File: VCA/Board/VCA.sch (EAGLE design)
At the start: 62 parts, among them IC1 TL074P, T1 BC237, T2 BC237, T3 BC237, T4 BC237, X1 1503_02, X2 1503_02, X3 1503_02, X4 1503_02

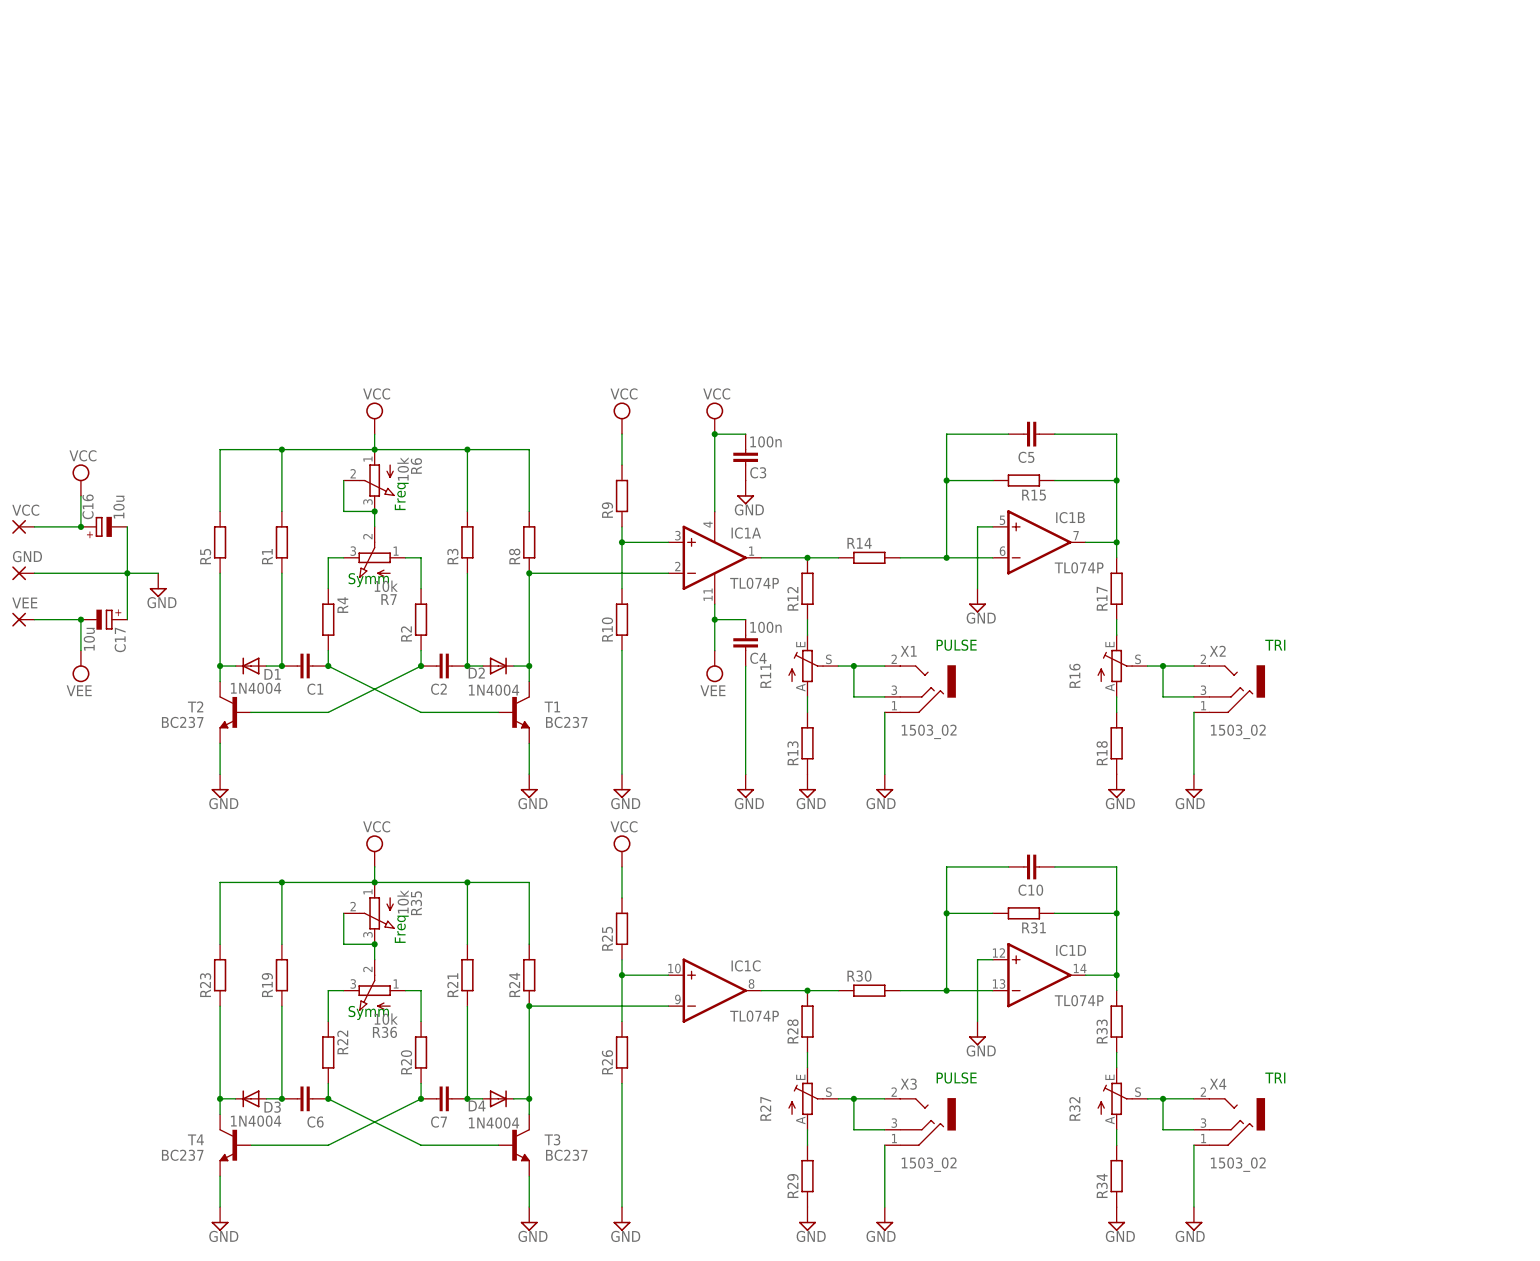
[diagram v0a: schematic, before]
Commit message: Add VCA schematic
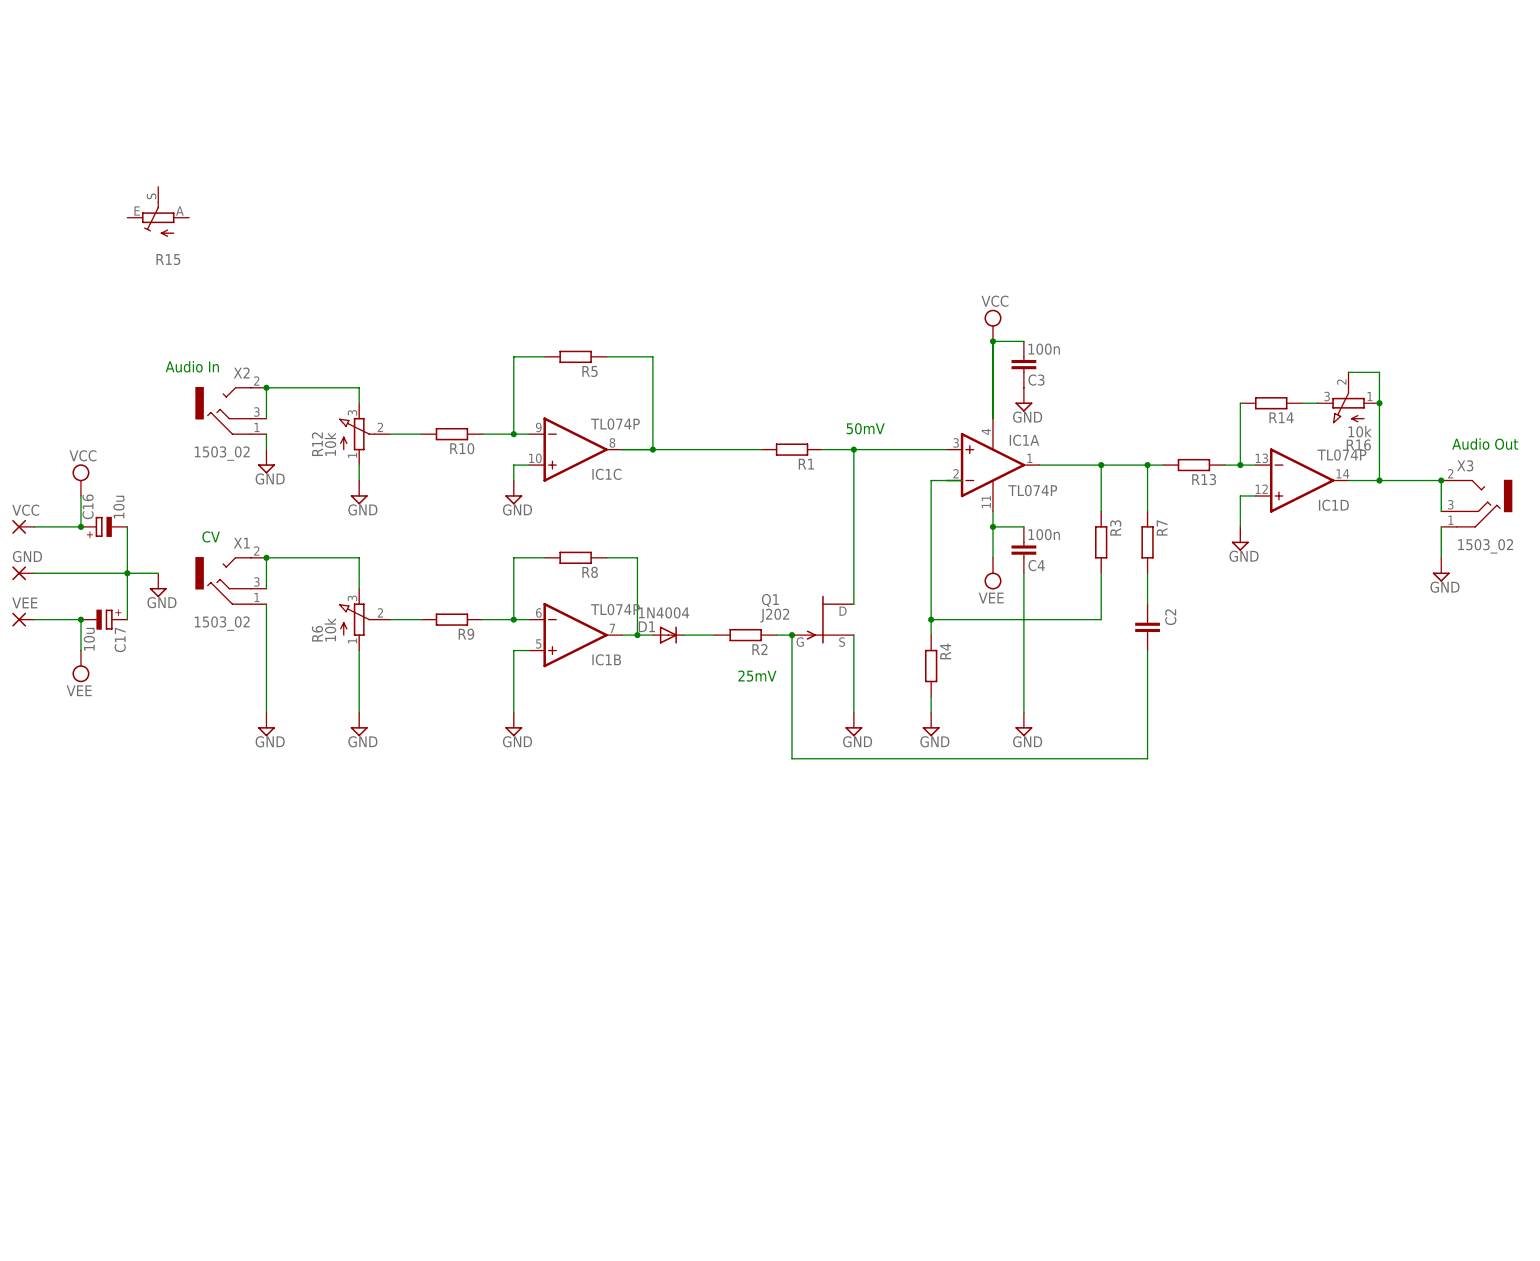
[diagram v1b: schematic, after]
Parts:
- removed C1, C10, C5, C6, C7: (no value), rcl:C-EU050-045X075
- removed D2, D3, D4: 1N4004, diode:1N4004
- removed R11, R27, R32: (no value), pot:TRIM_EU-S75P
- removed R17, R18, R19, R20, R21, R22, R23, R24, R25, R26, R28, R29, R30, R31, R33, R34: (no value), rcl:R-EU_0207/10
- removed R35, R36: 10k, pot:3RP/1610N
- removed T1, T2, T3, T4: BC237, transistor:BC237
- removed X4: 1503_02, con-lumberg:1503_02
- added Q1: J202, transistor-fet:J202
- R12: value (none) -> 10k; device rcl:R-EU_0207/10 -> pot:3RP/1610N
- R15: device rcl:R-EU_0207/10 -> pot:TRIM_EU-S75P
- R16: value (none) -> 10k; device pot:TRIM_EU-S75P -> pot:3RP/1610N
- R7: value 10k -> (none); device pot:3RP/1610N -> rcl:R-EU_0207/10
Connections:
- removed net N$18: D3.C, R23.1, T4.C
- removed net N$19: C6.2, D3.A, R19.1
- removed net N$20: R16.A, R18.2
- removed net N$21: R16.E, R17.1
- removed net N$22: C6.1, R22.2, T3.B
- removed net N$23: C7.2, R20.1, T4.B
- removed net N$24: C7.1, D4.A, R21.1
- removed net N$25: D4.C, IC1C.-IN, R24.1, T3.C
- removed net N$26: R22.1, R36.E
- removed net N$27: R20.2, R36.A
- removed net N$28: R35.E, R35.S, R36.S
- removed net N$29: IC1C.+IN, R25.1, R26.2
- removed net N$30: IC1C.OUT, R28.2, R30.1
- removed net N$31: R27.A, R29.2
- removed net N$32: R27.E, R28.1
- removed net N$33: C10.1, IC1D.OUT, R31.1, R33.2
- removed net N$34: C10.2, IC1D.-IN, R30.2, R31.2
- removed net N$35: R32.A, R34.2
- removed net N$36: R32.E, R33.1
- removed net N$37: R27.S, X3.2, X3.3
- removed net N$38: R32.S, X4.2, X4.3
- net GND: now also C3.1, C4.1, IC1C.+IN, Q1.S, R12.A, R4.2, R6.A; no longer R10.1, R13.1, R18.1, R26.1, R29.1, R34.1, T1.E, T2.E, T3.E, T4.E, X4.1
- net N$1: now also IC1A.+IN, Q1.D, R1.1; no longer C2.2, R2.1, T2.B
- net N$10: now also R12.E; no longer R16.S
- net N$11: now also IC1C.OUT, R1.2, R5.1; no longer IC1A.+IN, R10.2, R9.1
- net N$12: now also IC1C.-IN, R10.1, R5.2; no longer R11.A, R13.2
- net N$13: now also R10.2, R12.S; no longer IC1A.OUT, R12.2, R14.1
- net N$14: now also IC1D.-IN, R13.1, R14.2; no longer R11.E, R12.1
- net N$15: now also R6.E; no longer R11.S
- net N$16: now also R14.1, R16.E; no longer C5.1, IC1B.OUT, R15.1, R17.2
- net N$17: now also IC1D.OUT, R16.A, R16.S, X3.2, X3.3; no longer C5.2, IC1B.-IN, R14.2, R15.2
- net N$2: now also C2.2, Q1.G, R2.1; no longer C2.1, D2.A, R3.1
- net N$3: now also IC1A.-IN, R3.2, R4.1; no longer D1.C, R5.1, T2.C
- net N$4: now also IC1A.OUT, R13.2, R3.1, R7.1; no longer C1.2, D1.A, R1.1
- net N$5: now also C2.1, R7.2; no longer C1.1, R4.2, T1.B
- net N$6: now also R6.S, R9.2; no longer D2.C, IC1A.-IN, R8.1, T1.C
- net N$7: now also D1.A, IC1B.OUT, R8.1; no longer R4.1, R7.E
- net N$8: now also IC1B.-IN, R8.2, R9.1; no longer R2.2, R7.A
- net N$9: now also D1.C, R2.2; no longer R6.E, R6.S, R7.S
- net VCC: now also C3.2; no longer R1.2, R19.2, R21.2, R23.2, R24.2, R25.2, R3.2, R5.2, R8.2, R9.2
- net VEE: now also C4.2
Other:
- note added: "25mV"
- note added: "50mV"
- note added: "Audio In"
- note added: "Audio Out"
- note added: "CV"
- note removed: "Freq"
- note removed: "PULSE"
- note removed: "Symm"
- note removed: "TRI"
- moved on the sheet: C2, C3, C4, D1, IC1A, IC1B, IC1C, IC1D, R1, R10, R13, R14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

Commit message: Add clip indicator to VCA
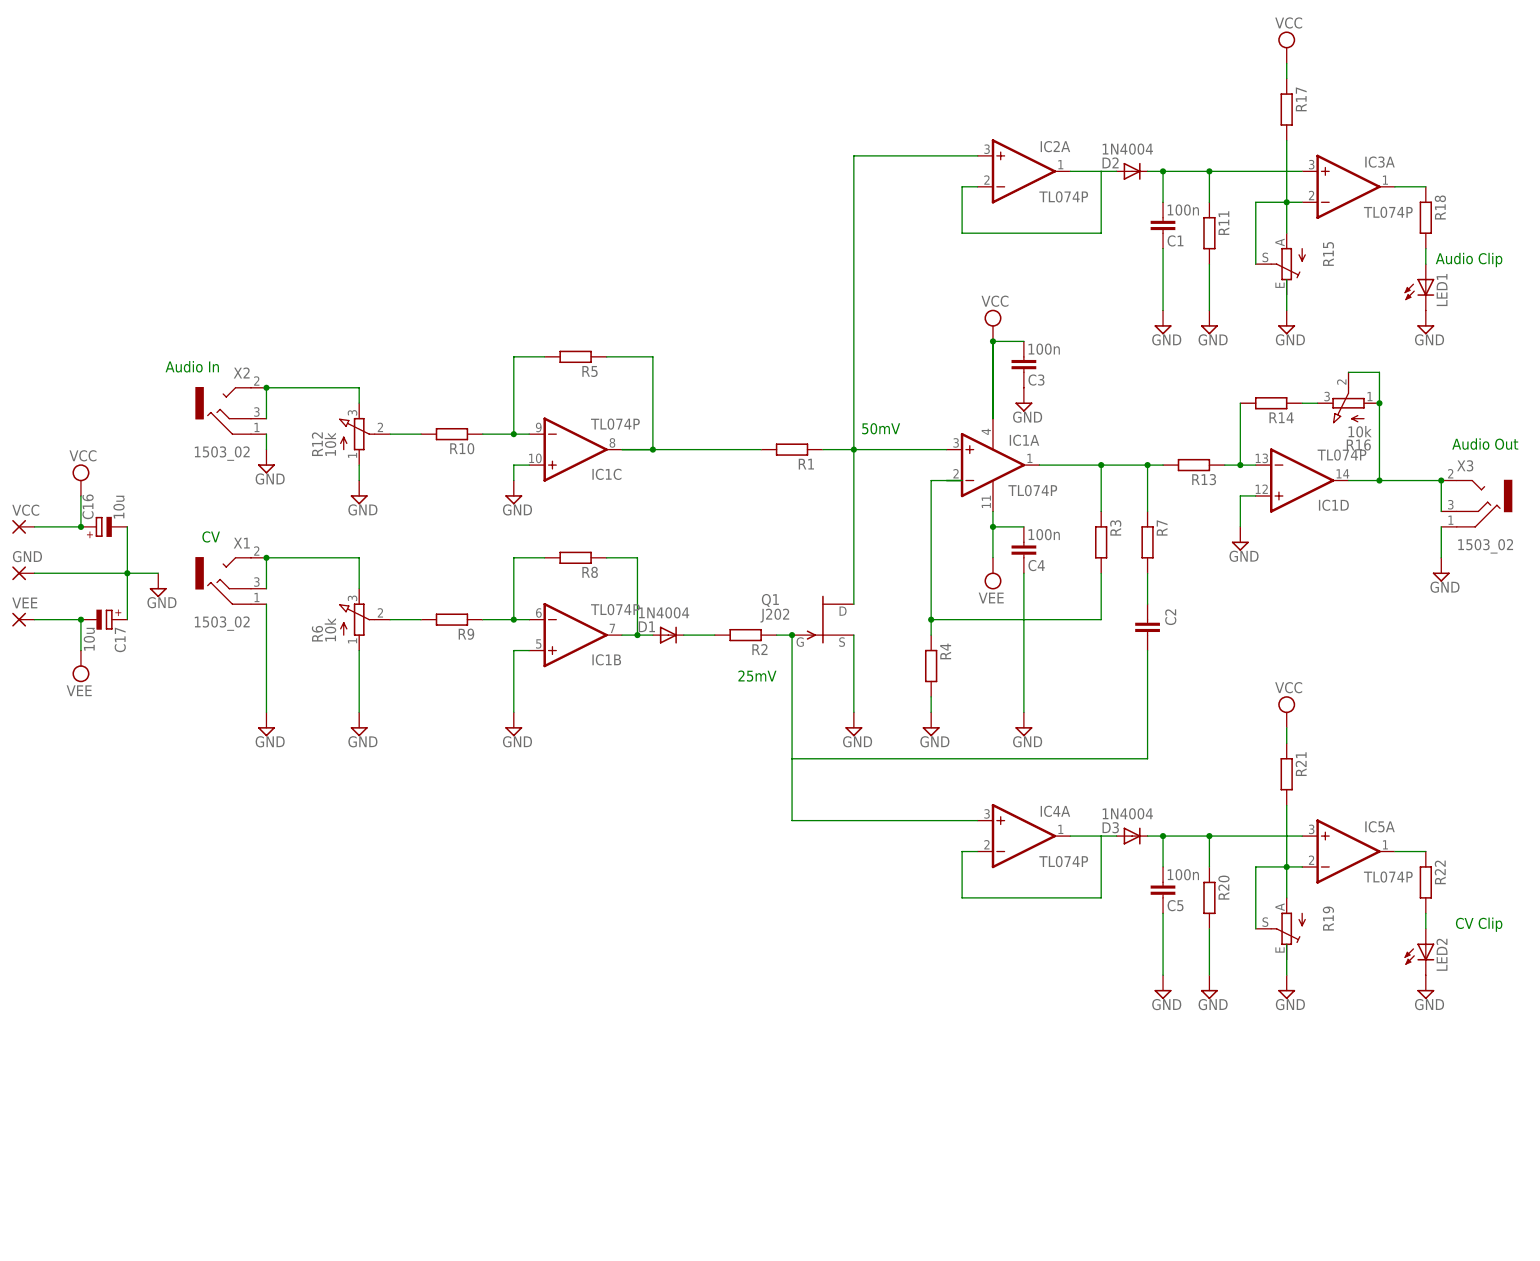
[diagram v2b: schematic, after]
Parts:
- added C1, C5: 100n, capacitor-wima:C5/2.5
- added D2, D3: 1N4004, diode:1N4004
- added IC2, IC3, IC4, IC5: TL074P, linear:TL074P
- added LED1, LED2: (no value), led:LED5MM
- added R11, R17, R18, R20, R21, R22: (no value), rcl:R-EU_0207/10
- added R19: (no value), pot:TRIM_EU-S75P
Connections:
- new net N$18: D2.A, IC2A.-IN, IC2A.OUT
- new net N$19: C1.2, D2.C, IC3A.+IN, R11.1
- new net N$20: IC3A.-IN, R15.A, R15.S, R17.2
- new net N$22: IC3A.OUT, R18.1
- new net N$23: LED1.A, R18.2
- new net N$25: D3.A, IC4A.-IN, IC4A.OUT
- new net N$26: C5.2, D3.C, IC5A.+IN, R20.1
- new net N$27: IC5A.-IN, R19.A, R19.S, R21.2
- new net N$28: IC5A.OUT, R22.1
- new net N$29: LED2.A, R22.2
- net GND: now also C1.1, C5.1, LED1.C, LED2.C, R11.2, R20.2
- net N$1: now also IC2A.+IN
- net N$2: now also IC4A.+IN
- net VCC: now also R17.1, R21.1
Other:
- note added: "Audio Clip"
- note added: "CV Clip"
- moved on the sheet: R15
